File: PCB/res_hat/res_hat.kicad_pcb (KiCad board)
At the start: 2 copper layers, 85 x 56 mm, 56 parts, among them IC1 DS1050Z-025+, IC2 DS1050Z-025+, IC3 UCC27324D, J1 Conn_02x20_Odd_Even, J10 Conn_01x02, J11 Jack-DC, J12 Conn_01x03, J2 Conn_02x04_Odd_Even, J3 Conn_01x03, J4 Conn_01x06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

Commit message: upgrade res hat to kicad 7.0
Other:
- net class Default removed

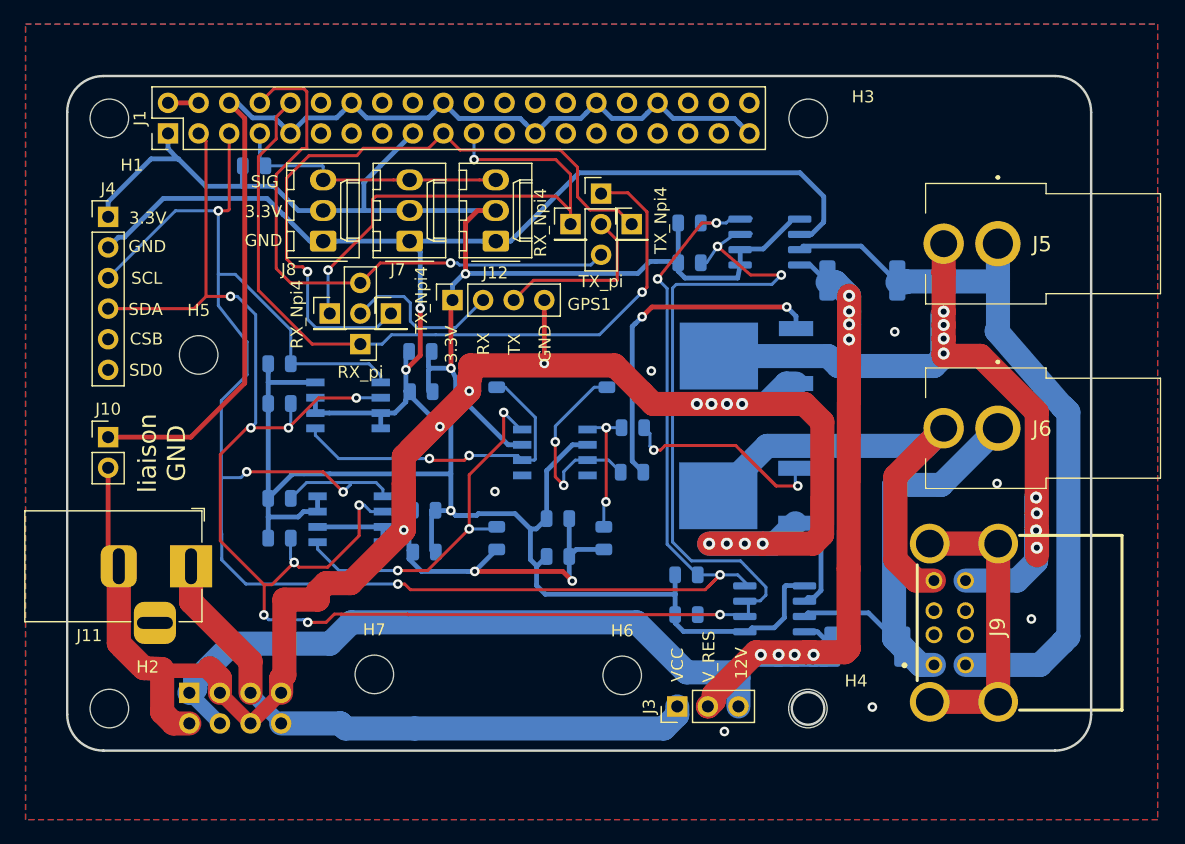
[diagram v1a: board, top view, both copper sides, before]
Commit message: upgrade relais hat and all hat to kicad 7.0
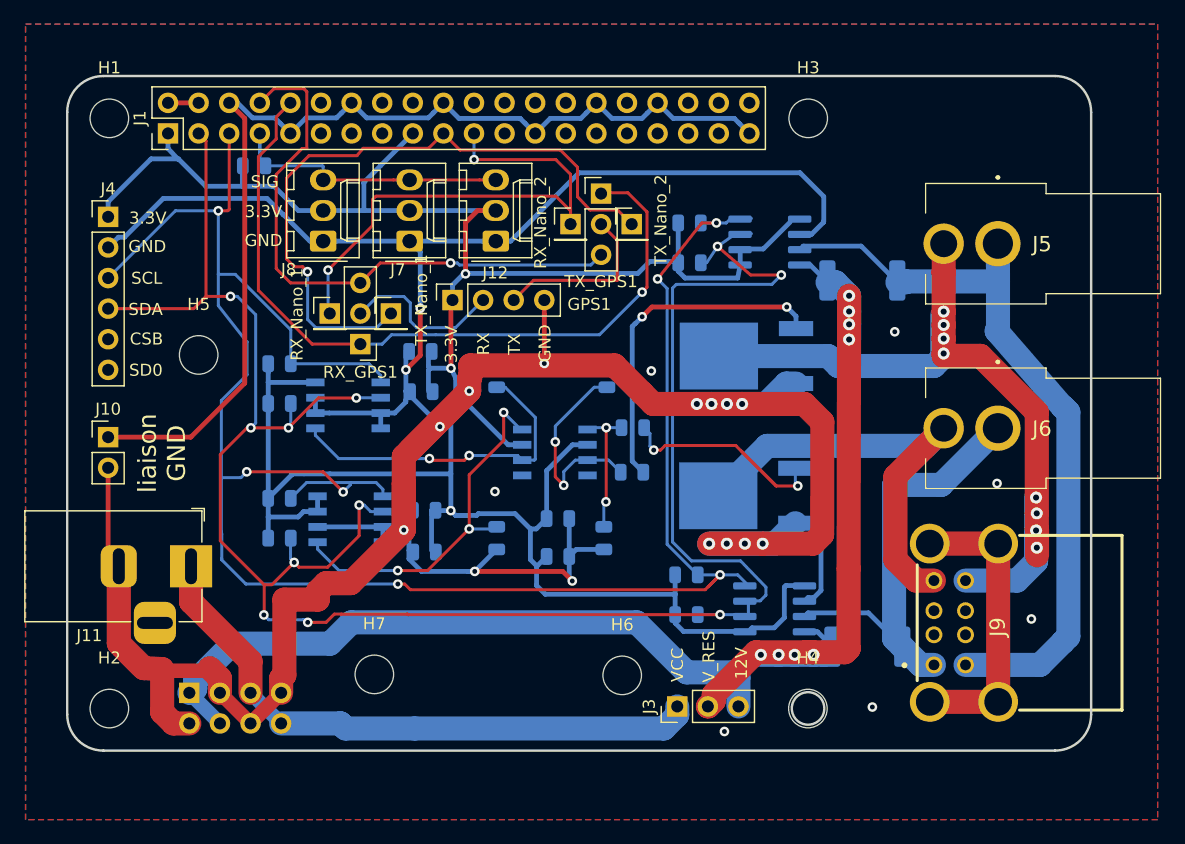
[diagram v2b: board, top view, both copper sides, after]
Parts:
- H1, H2, H3, H4, H5, H6, H7: footprint MountingHole:MountingHole_2.7mm_M2.5 -> MountingHole:MountingHole_3.2mm_M3
- renumbered RX_pi to RX_GPS1, RX_Npi4 to RX_Nano_1, RX_Npi4 to RX_Nano_2, TX_pi to TX_GPS1, TX_Npi4 to TX_Nano_1, TX_Npi4 to TX_Nano_2
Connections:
- C1 pad 2: +3V3 -> +3.3V
- C2 pad 2: +3V3 -> +3.3V
- C3 pad 2: +3V3 -> +3.3V
- C4 pad 2: +3V3 -> +3.3V
- GPS1 pad 1: +3V3 -> +3.3V
- IC1 pad 8: +3V3 -> +3.3V
- IC2 pad 7: +3V3 -> +3.3V
- IC2 pad 8: +3V3 -> +3.3V
- IC3 pad 1: (no net) -> unconnected-(IC3-N/A_1-Pad1)
- IC3 pad 8: (no net) -> unconnected-(IC3-N/A_2-Pad8)
- J1 pad 1: +3V3 -> +3.3V
- J1 pad 11: (no net) -> unconnected-(J1-Pin_11-Pad11)
- J1 pad 12: (no net) -> unconnected-(J1-Pin_12-Pad12)
- J1 pad 13: (no net) -> unconnected-(J1-Pin_13-Pad13)
- J1 pad 15: (no net) -> unconnected-(J1-Pin_15-Pad15)
- J1 pad 16: (no net) -> unconnected-(J1-Pin_16-Pad16)
- J1 pad 17: +3V3 -> +3.3V
- J1 pad 18: (no net) -> unconnected-(J1-Pin_18-Pad18)
- J1 pad 22: (no net) -> unconnected-(J1-Pin_22-Pad22)
- J1 pad 23: (no net) -> unconnected-(J1-Pin_23-Pad23)
- J1 pad 24: (no net) -> unconnected-(J1-Pin_24-Pad24)
- J1 pad 26: (no net) -> unconnected-(J1-Pin_26-Pad26)
- J1 pad 27: (no net) -> unconnected-(J1-Pin_27-Pad27)
- J1 pad 28: (no net) -> unconnected-(J1-Pin_28-Pad28)
- J1 pad 29: (no net) -> unconnected-(J1-Pin_29-Pad29)
- J1 pad 31: (no net) -> unconnected-(J1-Pin_31-Pad31)
- J1 pad 32: (no net) -> unconnected-(J1-Pin_32-Pad32)
- J1 pad 33: (no net) -> unconnected-(J1-Pin_33-Pad33)
- J1 pad 35: (no net) -> unconnected-(J1-Pin_35-Pad35)
- J1 pad 36: (no net) -> unconnected-(J1-Pin_36-Pad36)
- J1 pad 37: (no net) -> unconnected-(J1-Pin_37-Pad37)
- J1 pad 38: (no net) -> unconnected-(J1-Pin_38-Pad38)
- J1 pad 40: (no net) -> unconnected-(J1-Pin_40-Pad40)
- J12 pad 2: +3V3 -> +3.3V
- J4 pad 1: +3V3 -> +3.3V
- J4 pad 5: (no net) -> /CSB
- J4 pad 6: (no net) -> /SDO
- J7 pad 2: +3V3 -> +3.3V
- J8 pad 2: +3V3 -> +3.3V
- J9 pad 2: (no net) -> unconnected-(J9-Pin_2-Pad2)
- J9 pad 3: (no net) -> unconnected-(J9-Pin_3-Pad3)
- J9 pad 6: (no net) -> unconnected-(J9-Pin_6-Pad6)
- J9 pad 7: (no net) -> unconnected-(J9-Pin_7-Pad7)
- R1 pad 1: +3V3 -> +3.3V
- R15 pad 2: +3V3 -> +3.3V
- R2 pad 1: +3V3 -> +3.3V
- R3 pad 1: +3V3 -> +3.3V
- R4 pad 1: +3V3 -> +3.3V
- U1 pad 1: +3V3 -> +3.3V
- U1 pad 2: +3V3 -> +3.3V
- U1 pad 5: +3V3 -> +3.3V
- U2 pad 1: +3V3 -> +3.3V
- U2 pad 5: +3V3 -> +3.3V
